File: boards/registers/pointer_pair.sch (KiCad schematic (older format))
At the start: 21 parts

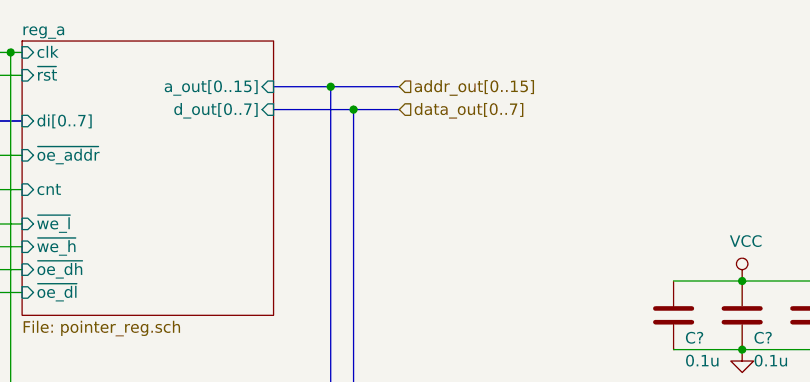
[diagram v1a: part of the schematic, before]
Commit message: Remove redundant chip from the register A, change hierarchical pin types
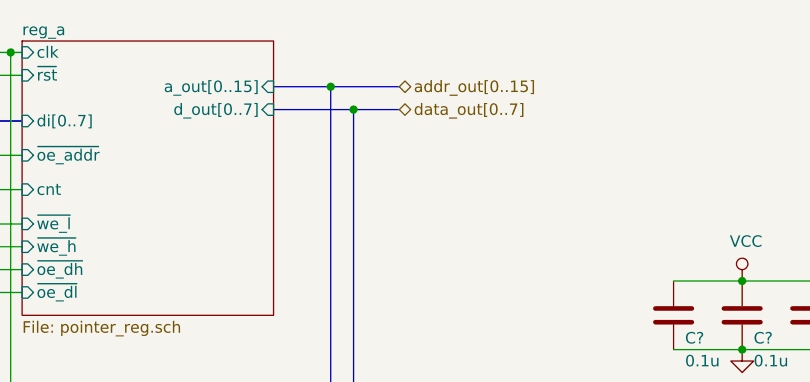
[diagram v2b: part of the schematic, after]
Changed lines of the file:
@@
 $Descr A4 11693 8268
 encoding utf-8
-Sheet 2 6
+Sheet 2 7
 Title "Pointer pair"
 Date "2019-12-28"
@@
 Text HLabel 1400 3000 0    50   Input ~ 0
 selector
-Text HLabel 8100 1650 2    50   Input ~ 0
+Text HLabel 8100 1650 2    50   3State ~ 0
 addr_out[0..15]
-Text HLabel 8100 1750 2    50   Input ~ 0
+Text HLabel 8100 1750 2    50   3State ~ 0
 data_out[0..7]
 $Sheet
@@
 U 1 1 5E5D26E3
 P 2950 5650
-F 0 "#PWR0101" H 2950 5400 50  0001 C CNN
+F 0 "#PWR?" H 2950 5400 50  0001 C CNN
 F 1 "GND" H 2955 5477 50  0000 C CNN
 F 2 "" H 2950 5650 50  0001 C CNN
@@
 U 1 1 5E5D37ED
 P 2950 3550
-F 0 "#PWR0102" H 2950 3400 50  0001 C CNN
+F 0 "#PWR?" H 2950 3400 50  0001 C CNN
 F 1 "VCC" H 2967 3723 50  0000 C CNN
 F 2 "" H 2950 3550 50  0001 C CNN
@@
 U 1 1 5E5D3E0B
 P 2450 4850
-F 0 "#PWR0103" H 2450 4600 50  0001 C CNN
+F 0 "#PWR?" H 2450 4600 50  0001 C CNN
 F 1 "GND" V 2455 4722 50  0000 R CNN
 F 2 "" H 2450 4850 50  0001 C CNN
@@
 U 1 1 5E5D47B1
 P 2450 4750
-F 0 "#PWR0104" H 2450 4500 50  0001 C CNN
+F 0 "#PWR?" H 2450 4500 50  0001 C CNN
 F 1 "GND" V 2455 4622 50  0000 R CNN
 F 2 "" H 2450 4750 50  0001 C CNN
@@
 U 1 1 5E5D4A87
 P 2450 4150
-F 0 "#PWR0105" H 2450 3900 50  0001 C CNN
+F 0 "#PWR?" H 2450 3900 50  0001 C CNN
 F 1 "GND" V 2455 4022 50  0000 R CNN
 F 2 "" H 2450 4150 50  0001 C CNN
@@
 U 1 1 5E5D4D08
 P 2450 4050
-F 0 "#PWR0106" H 2450 3800 50  0001 C CNN
+F 0 "#PWR?" H 2450 3800 50  0001 C CNN
 F 1 "GND" V 2455 3922 50  0000 R CNN
 F 2 "" H 2450 4050 50  0001 C CNN
@@
 U 1 1 5E5D4F67
 P 2450 4350
-F 0 "#PWR0107" H 2450 4100 50  0001 C CNN
+F 0 "#PWR?" H 2450 4100 50  0001 C CNN
 F 1 "GND" V 2455 4222 50  0000 R CNN
 F 2 "" H 2450 4350 50  0001 C CNN
@@
 U 1 1 5E5D5193
 P 2450 5050
-F 0 "#PWR0108" H 2450 4800 50  0001 C CNN
+F 0 "#PWR?" H 2450 4800 50  0001 C CNN
 F 1 "GND" V 2455 4922 50  0000 R CNN
 F 2 "" H 2450 5050 50  0001 C CNN
@@
 U 1 1 5E5D569A
 P 2450 5350
-F 0 "#PWR0109" H 2450 5100 50  0001 C CNN
+F 0 "#PWR?" H 2450 5100 50  0001 C CNN
 F 1 "GND" V 2455 5222 50  0000 R CNN
 F 2 "" H 2450 5350 50  0001 C CNN
@@
 U 1 1 5E5E1140
 P 3000 6800
-F 0 "#PWR0110" H 3000 6550 50  0001 C CNN
+F 0 "#PWR?" H 3000 6550 50  0001 C CNN
 F 1 "GND" H 3005 6627 50  0000 C CNN
 F 2 "" H 3000 6800 50  0001 C CNN
@@
 U 1 1 5E5E3388
 P 3000 6100
-F 0 "#PWR0111" H 3000 5950 50  0001 C CNN
+F 0 "#PWR?" H 3000 5950 50  0001 C CNN
 F 1 "VCC" H 3017 6273 50  0000 C CNN
 F 2 "" H 3000 6100 50  0001 C CNN
@@
 U 1 1 5E651ABF
 P 9350 4950
-F 0 "#PWR0112" H 9350 4700 50  0001 C CNN
+F 0 "#PWR?" H 9350 4700 50  0001 C CNN
 F 1 "GND" H 9355 4777 50  0000 C CNN
 F 2 "" H 9350 4950 50  0001 C CNN
@@
 U 1 1 5E651F92
 P 9350 3950
-F 0 "#PWR0113" H 9350 3800 50  0001 C CNN
+F 0 "#PWR?" H 9350 3800 50  0001 C CNN
 F 1 "VCC" H 9367 4123 50  0000 C CNN
 F 2 "" H 9350 3950 50  0001 C CNN
@@
 U 1 1 5E6558E9
 P 8600 4950
-F 0 "#PWR0114" H 8600 4700 50  0001 C CNN
+F 0 "#PWR?" H 8600 4700 50  0001 C CNN
 F 1 "GND" H 8605 4777 50  0000 C CNN
 F 2 "" H 8600 4950 50  0001 C CNN
@@
 U 1 1 5E6558EF
 P 8600 3950
-F 0 "#PWR0115" H 8600 3800 50  0001 C CNN
+F 0 "#PWR?" H 8600 3800 50  0001 C CNN
 F 1 "VCC" H 8617 4123 50  0000 C CNN
 F 2 "" H 8600 3950 50  0001 C CNN

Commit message: Control unit and ALU interfaces, gp_reg_a
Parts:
- removed Q?: 2N7002, Package_TO_SOT_SMD:SOT-23, symbol Transistor_FET:2N7002
- removed R?: 10k, symbol Device:R
- removed U?: 74LS153, symbol 74xx:74LS153
- added C?: 0.1u, symbol Device:C
- added U? (x4): 74HC86, symbol 74xx:74HC86
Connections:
- net labels added: addr_dp
- net labels removed: ~oe_addr_dp, ~oe_addr_ip
- wire segments 121 -> 123
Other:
- moved on the sheet: U?E

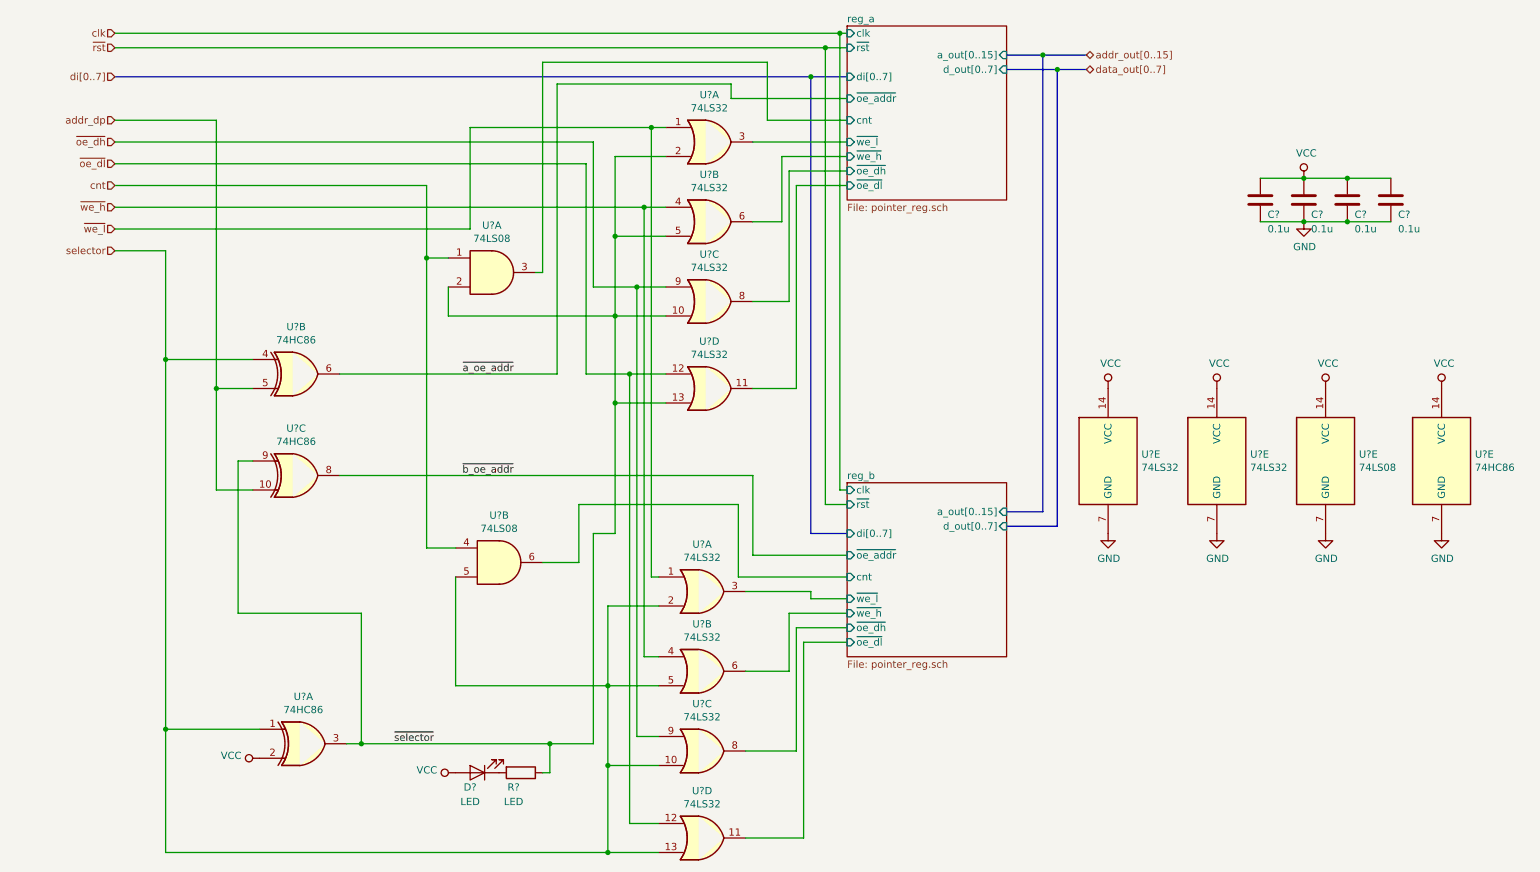
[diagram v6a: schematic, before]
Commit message: Annotated schematics, assigned footprints
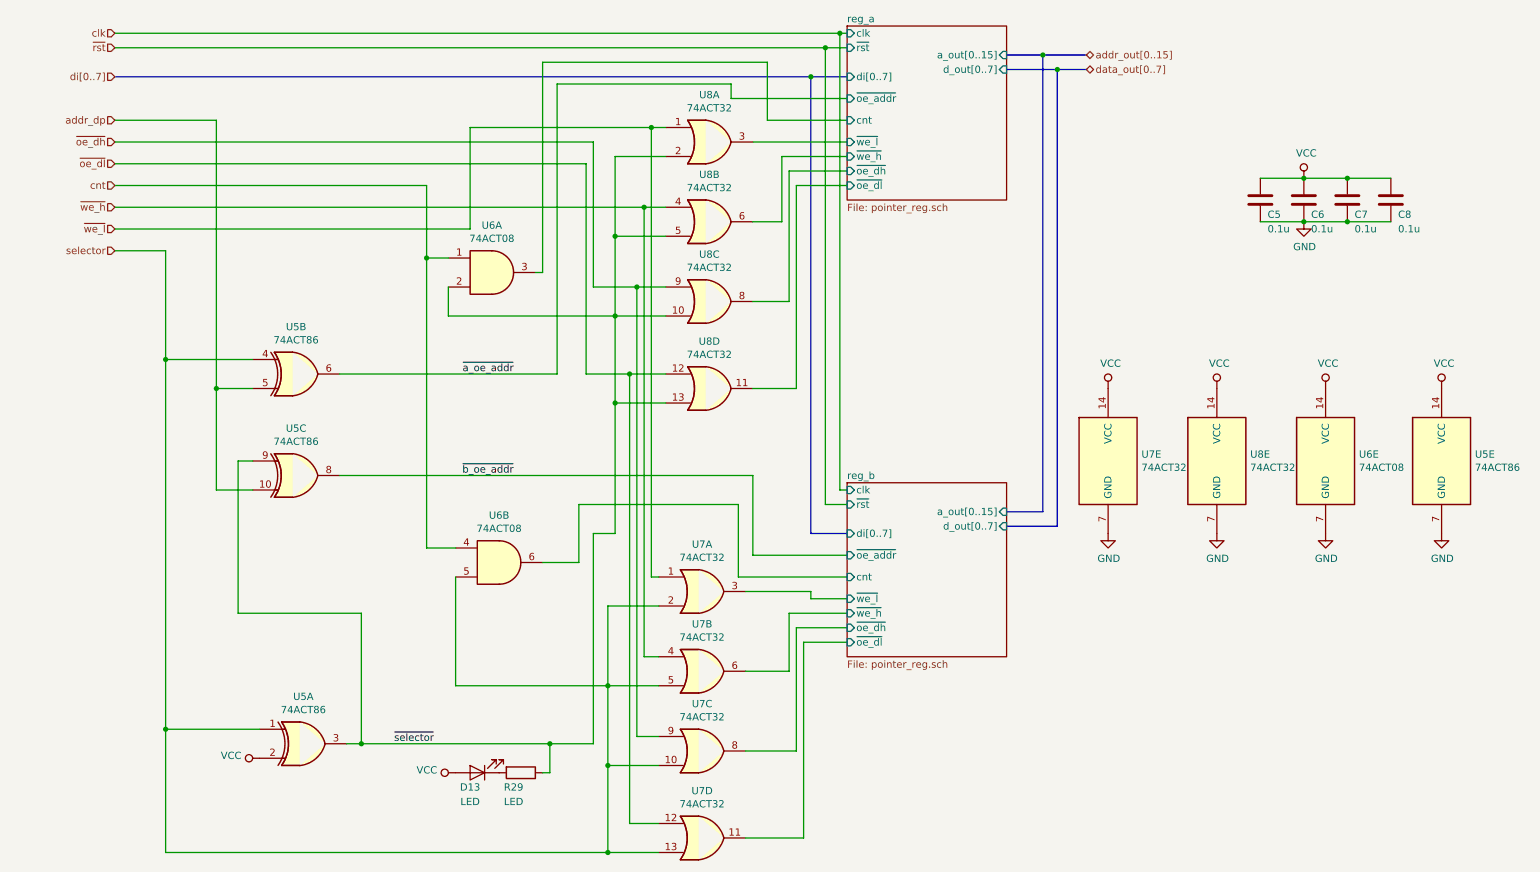
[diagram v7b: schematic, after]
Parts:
- C5, C6, C7, C8: renamed from C?; footprint (none) -> Capacitor_SMD:C_0805_2012Metric
- D13: renamed from D?; footprint (none) -> LED_SMD:LED_0805_2012Metric
- R29: renamed from R?; footprint (none) -> Resistor_SMD:R_0805_2012Metric
- U5: renamed from U?; value 74HC86 -> 74ACT86; footprint (none) -> Package_SO:SOIC-14_3.9x8.7mm_P1.27mm
- U6: renamed from U?; value 74LS08 -> 74ACT08; footprint (none) -> Package_SO:TSSOP-14_4.4x5mm_P0.65mm
- U7, U8: renamed from U?; value 74LS32 -> 74ACT32; footprint (none) -> Package_SO:TSSOP-14_4.4x5mm_P0.65mm

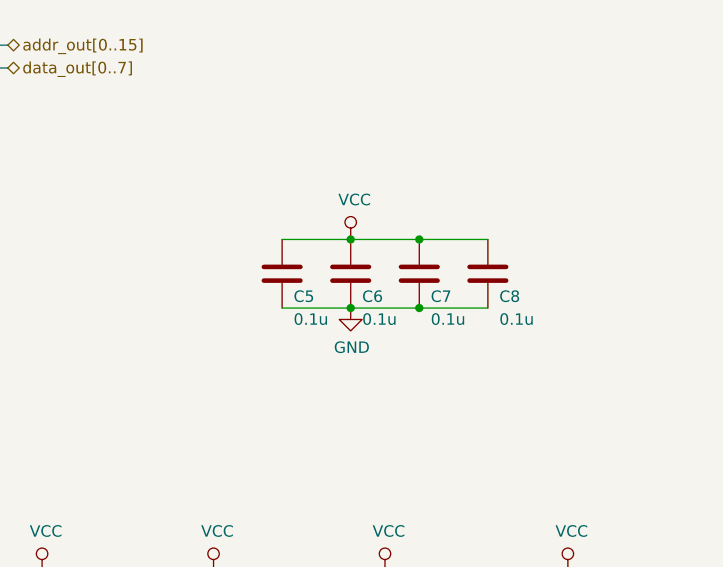
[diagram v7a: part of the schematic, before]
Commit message: CPU registers board
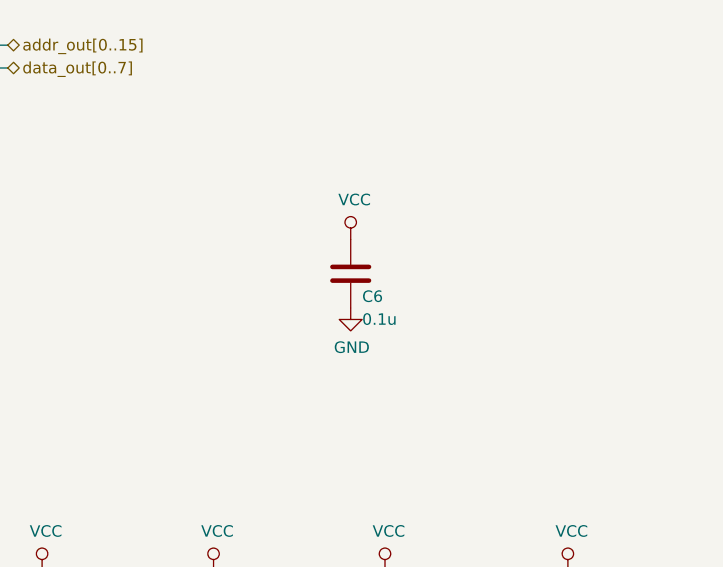
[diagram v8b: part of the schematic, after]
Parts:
- removed C5, C7, C8: 0.1u, Capacitor_SMD:C_0805_2012Metric, symbol Device:C
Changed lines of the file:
@@
 	6400 1500 6450 1500
-$Comp
-L Device:C C5
-U 1 1 5E6C09D7
-P 9300 2650
-F 0 "C5" H 9350 2550 50  0000 L CNN
-F 1 "0.1u" H 9350 2450 50  0000 L CNN
-F 2 "Capacitor_SMD:C_0805_2012Metric" H 9338 2500 50  0001 C CNN
-F 3 "~" H 9300 2650 50  0001 C CNN
-	1    9300 2650
-	1    0    0    -1
-$EndComp
 $Comp
 L Device:C C6
@@
 	1    0    0    -1
 $EndComp
-$Comp
-L Device:C C7
-U 1 1 5E6C302E
-P 9900 2650
-F 0 "C7" H 9950 2550 50  0000 L CNN
-F 1 "0.1u" H 9950 2450 50  0000 L CNN
-F 2 "Capacitor_SMD:C_0805_2012Metric" H 9938 2500 50  0001 C CNN
-F 3 "~" H 9900 2650 50  0001 C CNN
-	1    9900 2650
-	1    0    0    -1
-$EndComp
-Wire Wire Line
-	9300 2800 9600 2800
-Connection ~ 9600 2800
-Wire Wire Line
-	9600 2800 9900 2800
-Wire Wire Line
-	9900 2500 9600 2500
-Connection ~ 9600 2500
-Wire Wire Line
-	9600 2500 9300 2500
 $Comp
 L power:GND #PWR049
@@
 	1    0    0    -1
 $EndComp
-$Comp
-L Device:C C8
-U 1 1 5EBA32AE
-P 10200 2650
-F 0 "C8" H 10250 2550 50  0000 L CNN
-F 1 "0.1u" H 10250 2450 50  0000 L CNN
-F 2 "Capacitor_SMD:C_0805_2012Metric" H 10238 2500 50  0001 C CNN
-F 3 "~" H 10200 2650 50  0001 C CNN
-	1    10200 2650
-	1    0    0    -1
-$EndComp
-Wire Wire Line
-	10200 2500 9900 2500
-Connection ~ 9900 2500
-Wire Wire Line
-	9900 2800 10200 2800
-Connection ~ 9900 2800
 Text HLabel 1400 2100 0    50   Input ~ 0
 addr_dp
